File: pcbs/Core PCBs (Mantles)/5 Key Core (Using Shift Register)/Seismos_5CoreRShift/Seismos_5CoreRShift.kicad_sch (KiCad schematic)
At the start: 26 parts, among them IC1 74HC595, J1 SM010B-SRSS-TB(LF)(SN), J10 SM10B-SRSS-TB_(LF)(SN), J2 SM010B-SRSS-TB(LF)(SN), J3 SM010B-SRSS-TB(LF)(SN), J4 SM010B-SRSS-TB(LF)(SN), J5 SM010B-SRSS-TB(LF)(SN), J6 SM010B-SRSS-TB(LF)(SN), J7 SM09B-SRSS-TB(LF)(SN), J8 MJ-4PP-9-Lily58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

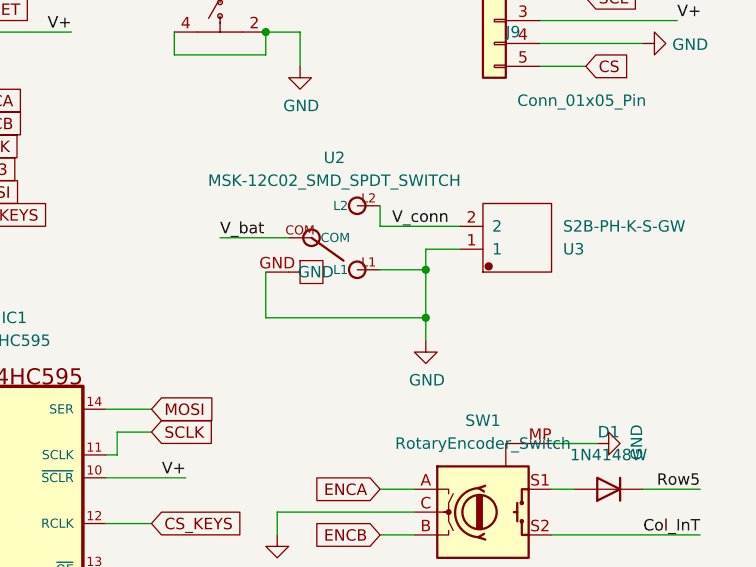
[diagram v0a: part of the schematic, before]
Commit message: HOTFIX, power switch bridges to ground
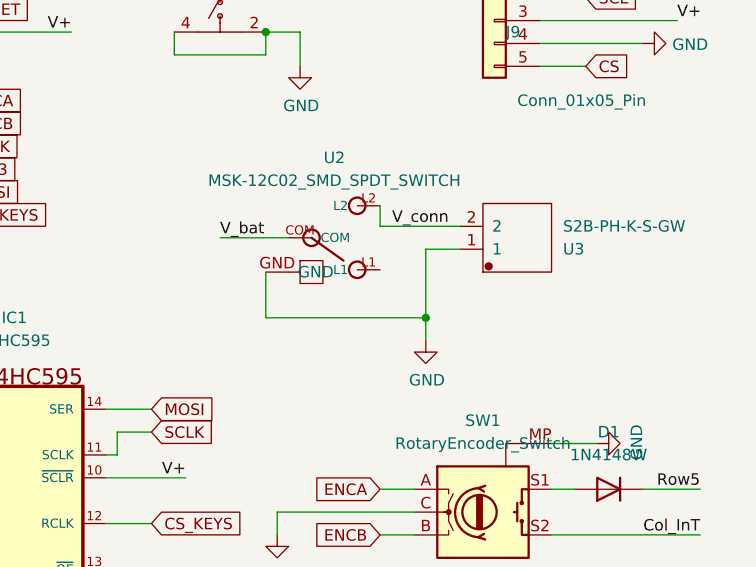
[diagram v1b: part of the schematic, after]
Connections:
- net GND: no longer U2.L1
